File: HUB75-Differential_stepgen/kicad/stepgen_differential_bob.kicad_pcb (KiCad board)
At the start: 2 copper layers, 85 x 56 mm, 35 parts, among them J1 Conn_02x08_Odd_Even, J2 Conn_02x08_Odd_Even, J3 Conn_02x08_Odd_Even, J4 Screw_Terminal_01x02, J5 RJ45_LED, J6 RJ45_LED, J7 RJ45_LED, SW1 SW_DIP_x03, SW2 SW_DIP_x03, U1 74HC86, U2 74HC86

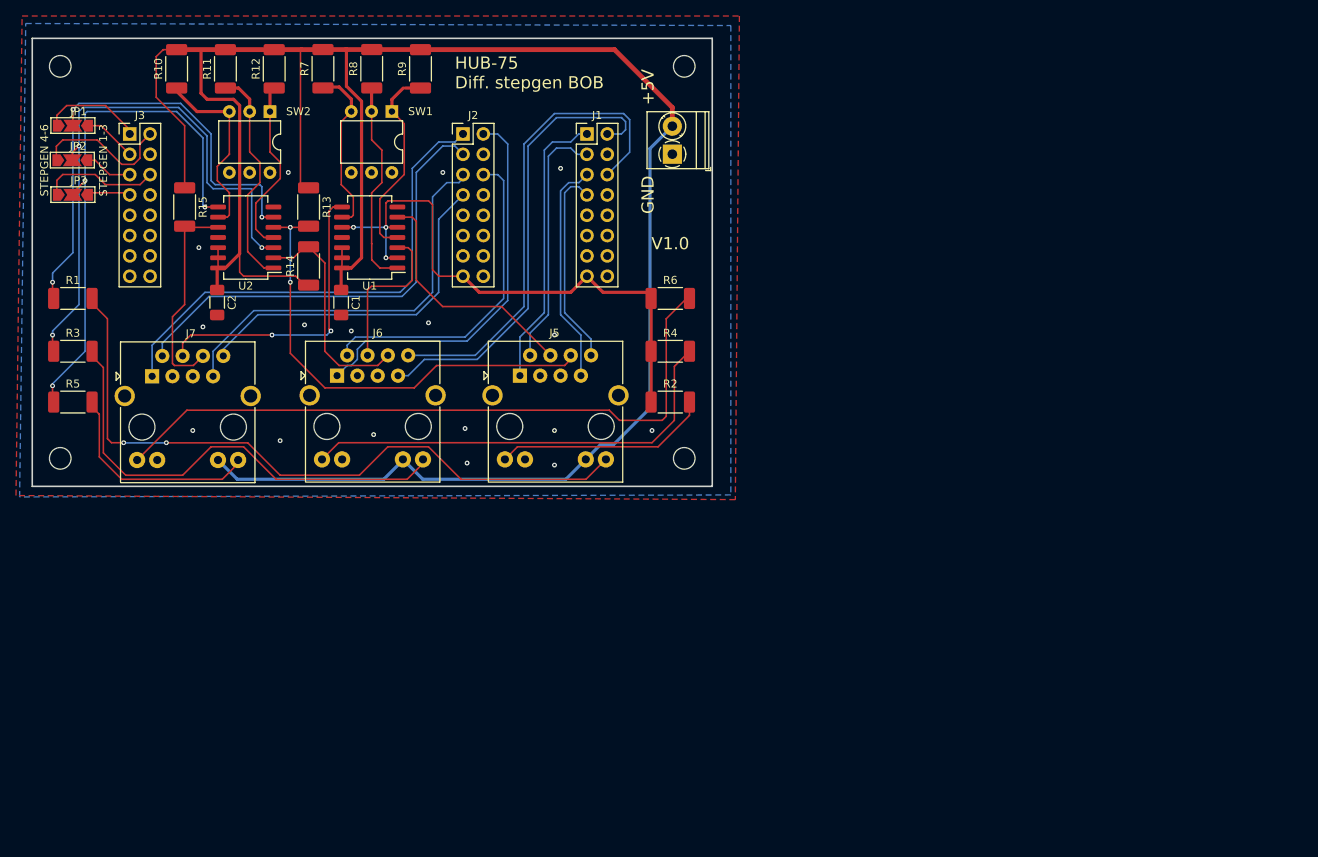
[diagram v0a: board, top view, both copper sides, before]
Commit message: Change trace width
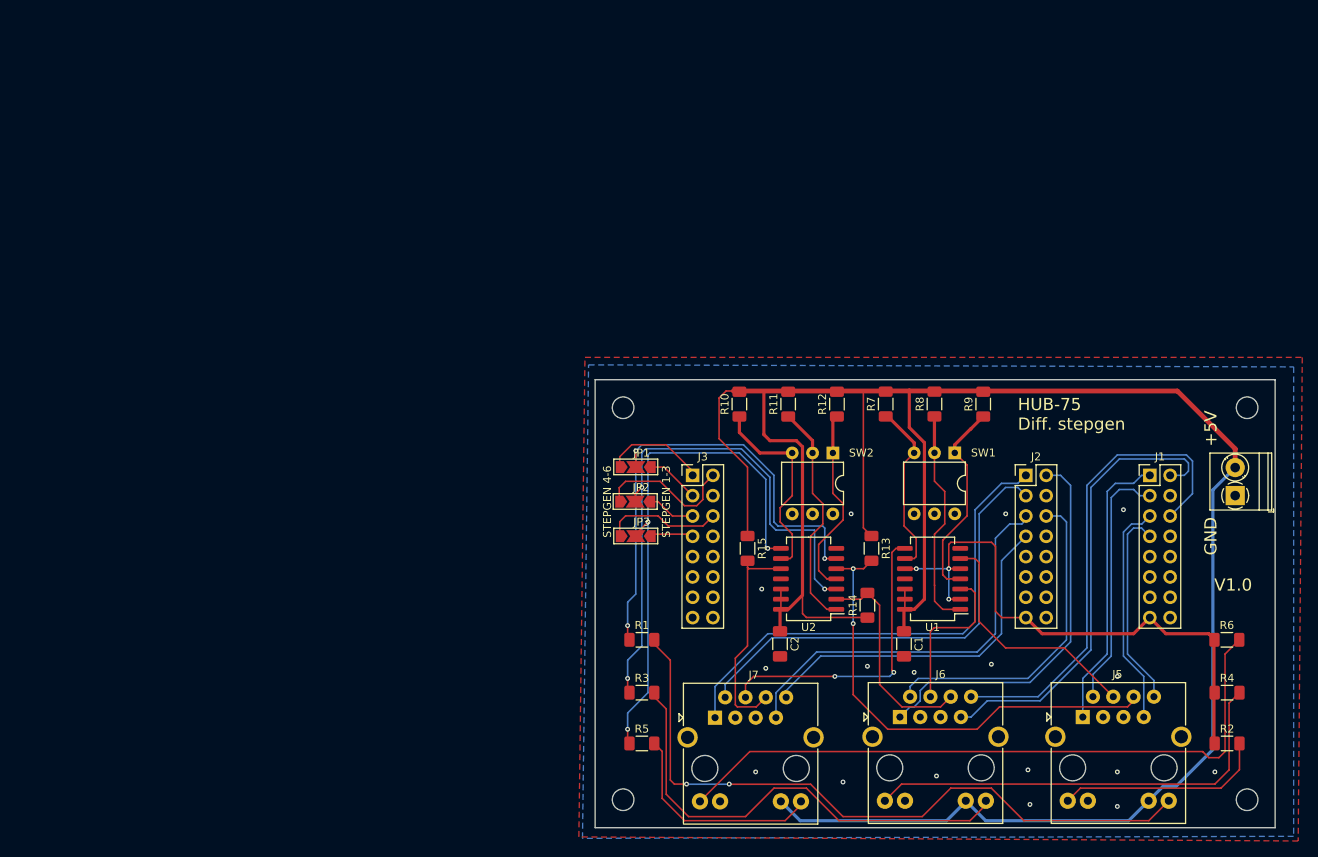
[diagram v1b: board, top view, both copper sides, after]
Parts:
- added G***: LOGO, LOGO, B.Cu at (140.5, 47.0)
- R1, R10, R11, R12, R13, R14, R15, R2, R3, R4, R5, R6, R7, R8, R9: footprint Resistor_SMD:R_2010_5025Metric_Pad1.40x2.65mm_HandSolder -> Resistor_SMD:R_1206_3216Metric_Pad1.30x1.75mm_HandSolder
- moved R1 82.9 mm to (76.2, 75.2)
- moved R3 82.9 mm to (76.2, 81.8)
- moved R5 82.9 mm to (76.2, 88.1)
- moved Hole1 82.3 mm to (151.9, 95.2)
- moved Hole2 82.3 mm to (151.9, 46.2)
- moved Hole3 82.3 mm to (73.9, 46.2)
- moved Hole4 82.3 mm to (73.9, 95.2)
- moved J3 82.3 mm to (82.5, 54.6)
- moved J5 82.3 mm to (131.3, 84.8)
- moved J6 82.3 mm to (108.5, 84.8)
- moved JP1 82.3 mm to (75.4, 53.6)
- moved JP3 82.3 mm to (75.4, 62.2)
- moved R13 82.3 mm to (104.9, 63.8)
- moved R15 82.3 mm to (89.4, 63.8)
- moved SW1 82.3 mm to (115.3, 51.8)
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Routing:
- net Net-(J7-Pad12): track 85.6 -> 83.5 mm
- net +5V: track 286.6 -> 288.5 mm
- net Net-(R8-Pad1): track 26.2 -> 27.8 mm
- net Net-(R10-Pad1): track 23.8 -> 25.4 mm
- net Net-(R12-Pad1): track 22.3 -> 23.9 mm
- net Net-(J7-Pad9): track 25.4 -> 26.6 mm
- net ALARM3: track 26.4 -> 27.3 mm
- net ALARM1: track 58.0 -> 58.9 mm
- net Net-(R9-Pad1): track 25.0 -> 25.7 mm
- net Net-(R11-Pad1): track 27.9 -> 28.6 mm
- net Net-(J5-Pad12): track 27.0 -> 26.3 mm
- net Net-(J6-Pad12): track 55.5 -> 54.8 mm
- net ALARM2: track 27.5 -> 26.9 mm
- net ALARM_OK3: track 66.1 -> 65.5 mm
- net ALARM_OK2: track 71.6 -> 71.0 mm
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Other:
- board text added: "By Peter van Tol"
- board text added: "HUB-75 Diff. stepgen"
- board text removed: "HUB-75 Diff. stepgen BOB"

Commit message: Update to v1.1 after prototype
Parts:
- J1, J2, J3: footprint Connector_PinHeader_2.54mm:PinHeader_2x08_P2.54mm_Vertical -> Connector_IDC:IDC-Header_2x08_P2.54mm_Vertical
- R1, R2, R3, R4, R5, R6: value 290 -> 270
- moved JP3 5.08 mm to (75.2, 67.3)
- moved JP1 5.08 mm to (75.2, 58.7)
- moved JP2 5.08 mm to (75.1, 63.0)
- moved R15 1.27 mm to (90.7, 63.8)
- moved J3 0.78 mm to (83.3, 54.6)
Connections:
- J3 pad 1: DRIVE_OK_EXT4 -> DRIVE_OK_EXT1
- J3 pad 2: DRIVE_OK_EXT5 -> DRIVE_OK_EXT2
- J3 pad 3: DRIVE_OK_EXT1 -> DRIVE_OK_EXT3
- J3 pad 5: DRIVE_OK_EXT2 -> DRIVE_OK_EXT4
- J3 pad 6: DRIVE_OK_EXT6 -> DRIVE_OK_EXT5
- J3 pad 7: DRIVE_OK_EXT3 -> DRIVE_OK_EXT6
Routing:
- net DRIVE_OK_EXT3: track 5.22 -> 12.7 mm, vias 0 -> 1
- net DRIVE_OK_EXT2: track 5.92 -> 13.3 mm
- net DRIVE_OK_EXT4: track 12.9 -> 19.8 mm
- net ALARM_OK3: track 65.5 -> 64.5 mm
- net DRIVE_OK_EXT6: track 14.6 -> 15.4 mm
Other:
- board text added: "ALARM"
- board text added: "INV. ALARM"
- board text added: "INV. ENABLE"
- board text added: "V1.1"
- board text removed: "V1.0"
